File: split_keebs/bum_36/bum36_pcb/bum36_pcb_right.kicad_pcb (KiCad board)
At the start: 2 copper layers, 133.2 x 106.5 mm, 55 parts, among them J1 Battery JST, J2 USB_C_Receptacle_USB2.0_16P, SW1 SW_Push, SW10 SW_Push, SW11 SW_Push, SW12 SW_Push, SW13 SW_Push, SW14 SW_Push, SW15 SW_Push, SW16 SW_Push, SW17 SW_Push, SW18 SW_Push, SW19 RotaryEncoder_Switch, SW2 SW_Push, SW20 SW_SPDT, SW21 SW_Push, SW3 SW_Push, SW4 SW_Push, SW5 SW_Push, SW6 SW_Push, SW7 SW_Push, SW8 SW_Push, SW9 SW_Push, U1 nice_nano

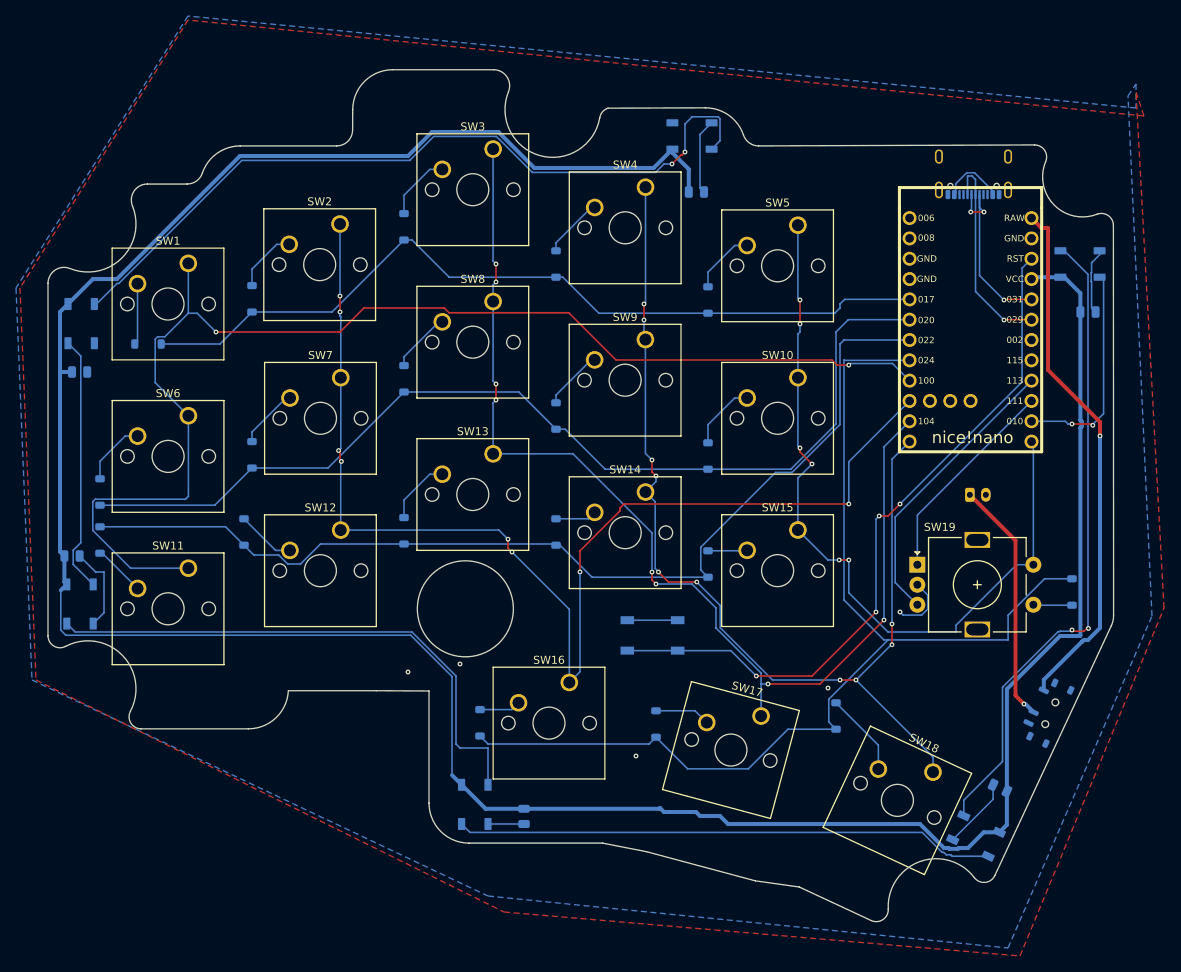
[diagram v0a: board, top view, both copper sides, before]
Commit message: added dxf to right pcb
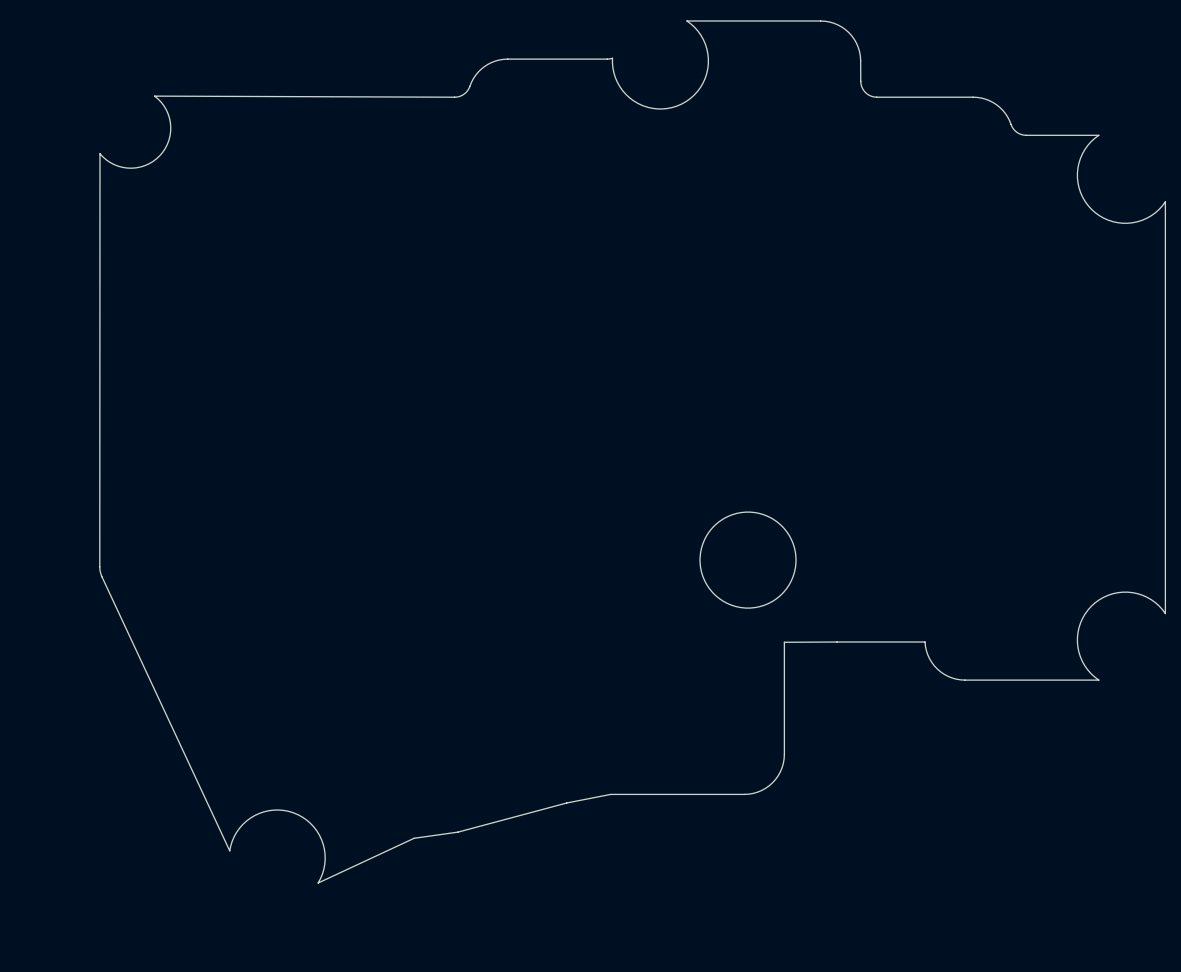
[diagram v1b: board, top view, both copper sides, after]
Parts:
- removed C1, C2, C3, C4, C5, C6: 0.1uF, Capacitor_SMD:C_0805_2012Metric
- removed D1, D10, D11, D12, D13, D14, D15, D16, D17, D18, D19, D2, D3, D4, D5, D6, D7, D8, D9: D, Diode_SMD:D_SOD-123
- removed J1: Battery JST, Connector_JST:JST_PH_B2B-PH-K_1x02_P2.00mm_Vertical
- removed J2: USB_C_Receptacle_USB2.0_16P, Connector_USB:USB_C_Receptacle_GCT_USB4105-xx-A_16P_TopMnt_Horizontal
- removed LED1, LED2, LED3, LED4, LED5, LED6: WS2812B, LED_SMD:LED_WS2812B_PLCC4_5.0x5.0mm_P3.2mm
- removed SW1, SW10, SW11, SW12, SW13, SW14, SW15, SW16, SW17, SW18, SW2, SW3, SW4, SW5, SW6, SW7, SW8, SW9: SW_Push, Button_Switch_Keyboard:SW_Cherry_MX_1.00u_PCB
- removed SW19: RotaryEncoder_Switch, Rotary_Encoder:RotaryEncoder_Alps_EC11E-Switch_Vertical_H20mm
- removed SW20: SW_SPDT, Button_Switch_SMD:SW_SPDT_Shouhan_MSK12C02
- removed SW21: SW_Push, Button_Switch_SMD:SW_SPST_TL3342
- removed U1: nice_nano, nice-nano-kicad-master:nice_nano
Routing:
- net /LED_VCC: track 353.9 -> 0.00 mm
- net /COL0: track 159.1 -> 0.00 mm, vias 2 -> 0
- net /COL1: track 150.3 -> 0.00 mm, vias 8 -> 0
- net /COL2: track 138.7 -> 0.00 mm, vias 8 -> 0
- net /ROW3: track 137.3 -> 0.00 mm
- net /COL3: track 130.1 -> 0.00 mm, vias 10 -> 0
- net /ROW2: track 127.5 -> 0.00 mm
- net /ROW1: track 125.5 -> 0.00 mm
- net /ROW0: track 103.7 -> 0.00 mm
- net Net-(LED5-DOUT): track 98.0 -> 0.00 mm, vias 2 -> 0
- net /COL4: track 96.3 -> 0.00 mm, vias 6 -> 0
- net Net-(U1-RST): track 88.6 -> 0.00 mm, vias 4 -> 0
- net Net-(LED1-DOUT): track 80.4 -> 0.00 mm, vias 2 -> 0
- net Net-(LED3-DOUT): track 68.7 -> 0.00 mm
- net Net-(LED2-DOUT): track 67.5 -> 0.00 mm
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- removed copper zone on B.Cu, net /GND
- removed copper zone on F.Cu, net /GND
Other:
- board size 133.2 x 106.5 mm -> 133.2 x 107.8 mm
